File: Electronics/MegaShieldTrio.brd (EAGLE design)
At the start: 99.8 x 80 mm, 29 parts, among them J2 RJ11-2L-B, X1 RJ45-6L21-B, X2 Cruise

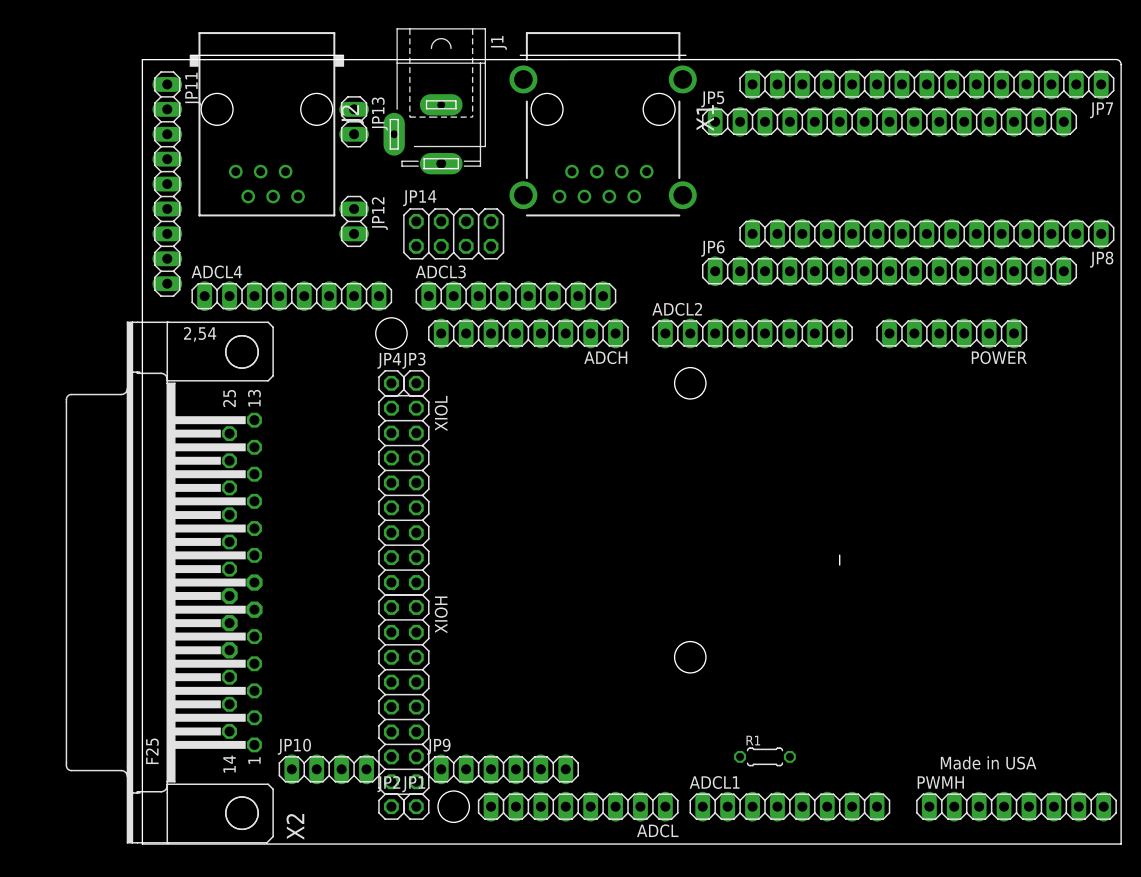
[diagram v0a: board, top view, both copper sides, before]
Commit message: New sonar board; trio modified to match
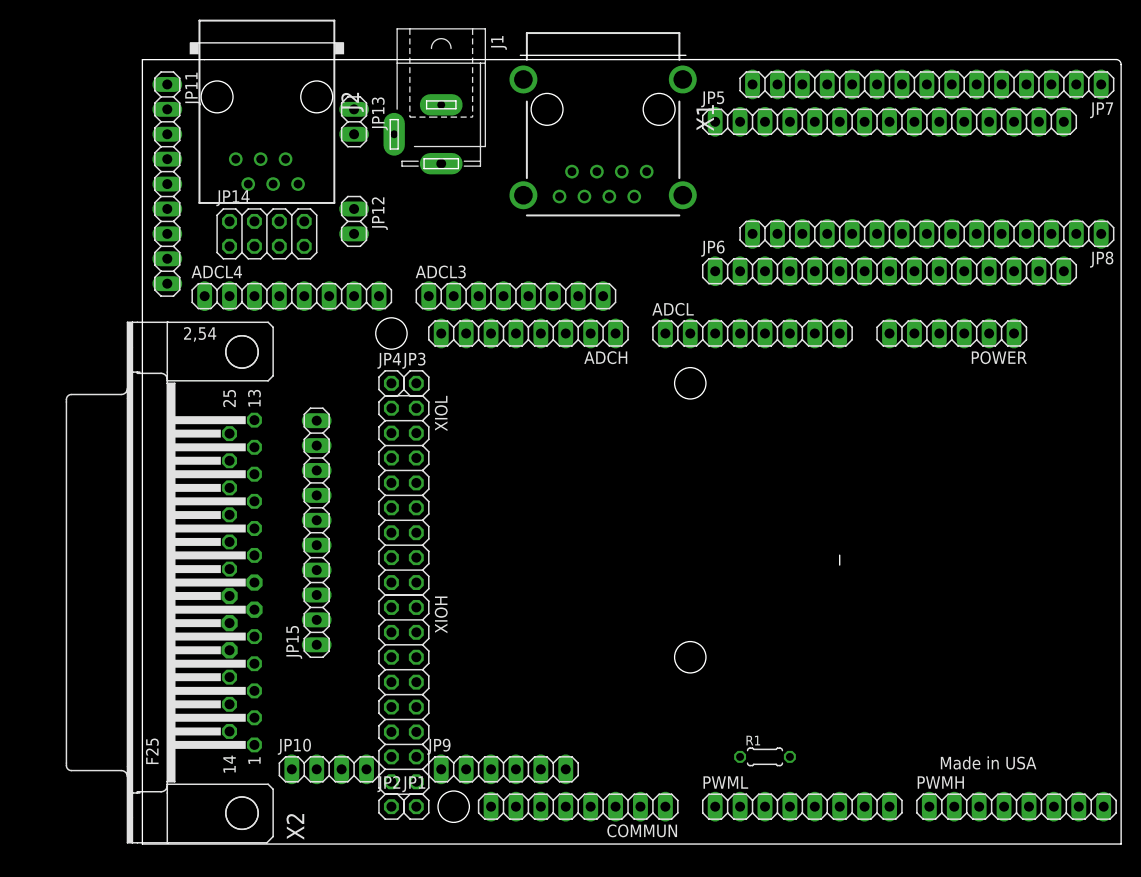
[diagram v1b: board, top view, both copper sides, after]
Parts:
- removed ADCL1: Digital 0-7, pinhead:1X08
- removed ADCL2: Analog In 0-7, pinhead:1X08
- added COMMUN: Digital 14-21, pinhead:1X08
- added JP15: (no value), pinhead:1X10
- added PWML: Digital 0-7, pinhead:1X08
- ADCL: value Digital 14-21 -> Analog In 0-7
- moved ADCL 51.4 mm to (62.2, 52.1), turned to 0 degrees
- moved JP14 19.1 mm to (12.7, 62.2)
- moved J2 1.27 mm to (12.7, 76.2)
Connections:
- new net N$2: COMMUN.2, PWML.3
- new net N$9: COMMUN.1, PWML.4
- net +5V: now also X1.1; no longer X1.2
- net A6: now also COMMUN.7; no longer ADCL.7
- net D3INT1: now also COMMUN.8; no longer ADCL.8
- net GND: now also X1.4; no longer X1.1
- net N$1: now also PWML.1; no longer ADCL1.1
- net N$11: now also COMMUN.4; no longer ADCL.4
- net N$25: now also ADCL.5, X1.7; no longer ADCL2.5, X1.5
- net N$26: now also ADCL.6, X1.3; no longer ADCL2.6, X1.6
- net N$33: now also COMMUN.3; no longer ADCL.3
- net N$34: now also ADCL.7, X1.5; no longer ADCL2.7, X1.7
- net N$35: now also ADCL.8; no longer ADCL2.8
- net N$36: now also X1.2; no longer X1.3
- net N$37: now also PWML.2; no longer ADCL1.2
- net N$7: now also ADCL.4, X1.6; no longer ADCL2.4, X1.4

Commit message: Parts match physical size
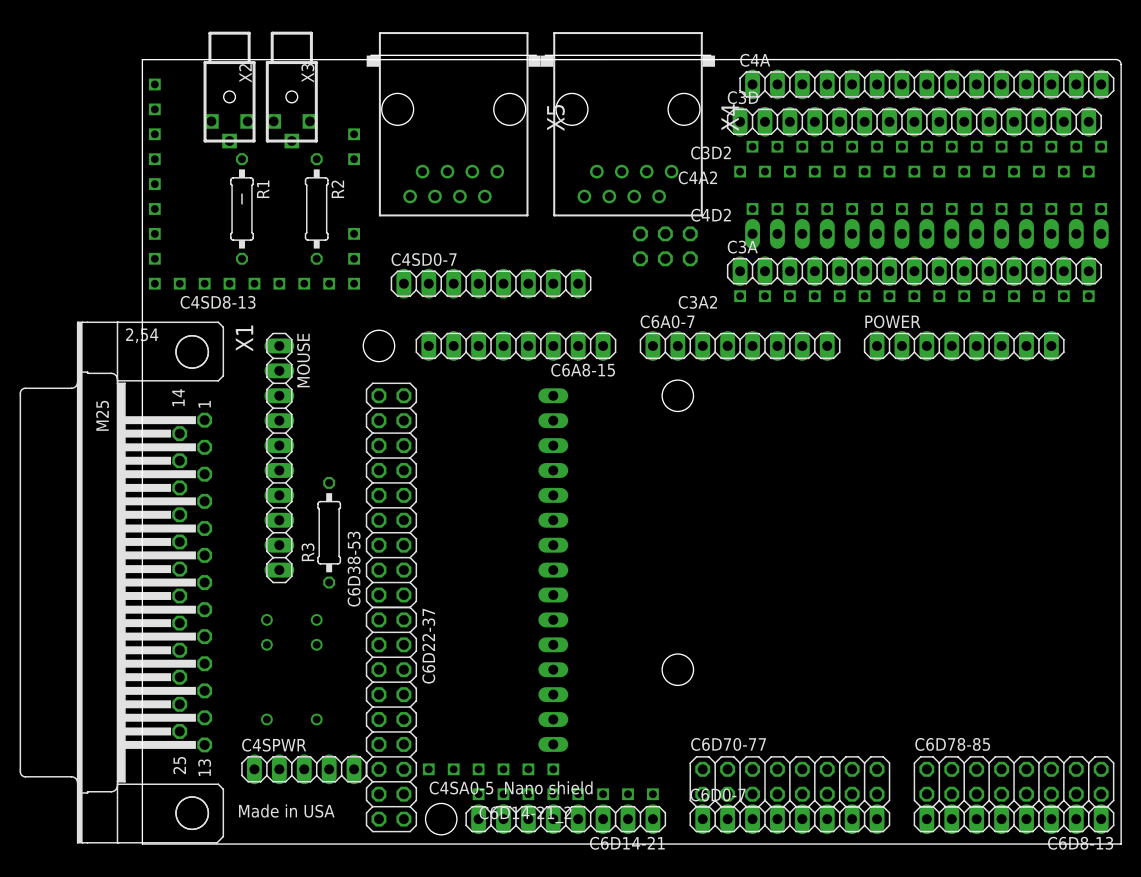
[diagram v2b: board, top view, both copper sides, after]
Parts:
- removed ADCH: Analog In 8-15, pinhead:1X08
- removed ADCL: Analog In 0-7, pinhead:1X08
- removed ADCL3, PWML: Digital 0-7, pinhead:1X08
- removed ADCL4, PWMH: Digital 8-13, pinhead:1X08
- removed COMMUN: Digital 14-21, pinhead:1X08
- removed J1: (no value), con-jack:SPC4077
- removed J2: RJ11-2L-B, con-tycoelectronics:RJ11-NO_SHIELD
- removed JP1, JP2: 5V, pinhead:1X01
- removed JP10: (no value), pinhead:1X04
- removed JP11: (no value), pinhead:1X09
- removed JP12, JP13: (no value), pinhead:1X02
- removed JP14: (no value), pinhead:2X04
- removed JP15: (no value), pinhead:1X10
- removed JP3, JP4: GND, pinhead:1X01
- removed JP5: C3 Digital, pinhead:1X15
- removed JP6: C3 Analog, pinhead:1X15
- removed JP9: (no value), pinhead:1X06
- removed XIOH: Digital 22-37, pinhead:2X08
- removed XIOL: Digital 38-53, pinhead:2X08
- added C3A: C3 Analog, pinhead:1X15
- added C3A2, C3D2, C4A2, C4D2: 1X15HEADER, Elcano:1X15HEADER
- added C3D: C3 Digital, pinhead:1X15
- added C4SA0-5: Nano shield, Elcano:1X6HEADER
- added C4SD0-7: Nano shield, pinhead:1X08
- added C4SD8-13: Nano shield, Elcano:1X8HEADER
- added C4SPWR: Nano shield, pinhead:1X05
- added C5A: C5 Analog, pinhead:1X15
- added C6A0-7: C6 Analog In 0-7, pinhead:1X08
- added C6A8-15: C6 Analog In 8-15, pinhead:1X08
- added C6D0-7: GPS, pinhead:1X08
- added C6D14-21: C6 Digital 14-21, pinhead:1X08
- added C6D14-21_2: C5D, Elcano:1X8HEADER
- added C6D22-37: C6 Digital 22-37, pinhead:2X09
- added C6D38-53: C6 Digital 38-53, pinhead:2X09
- added C6D70-77, C6D78-85: Max32, pinhead:2X08
- added C6D8-13: C6D8-13, pinhead:1X08
- added ICSP: (no value), pinhead:2X03
- added MOUSE: Visual odometry, pinhead:1X10
- added R2, R3: 1 M, rcl:0207/10
- added RL1: V23040--B201TSC, Elcano:TSC-112L3H
- added U$4: CHR_UM6, Elcano:CHR_UM6
- added X3: ODO_JACK, Elcano:ODO_JACK
- added X4, X5: RJ45-8L-B, con-tycoelectronics:RJ45-NO-SHIELD
- C4A: value C4 Digital -> C4 Analog
- C4D: value C4 Analog -> C4 Digital
- POWER: value POWER -> C6 Power; device pinhead:1X06 -> pinhead:1X08
- R1: value 1M -> 1 M; device rcl:0204/5 -> rcl:0207/10
- X1: value RJ45-6L21-B -> Vehicle control; device con-tycoelectronics:RJ45-SHIELD1 -> con-subd:M25H
- X2: value Cruise -> ODO_JACK; device con-subd:F25H -> Elcano:ODO_JACK
- moved R1 77.3 mm to (10.2, 64.8), turned to 270 degrees
- moved X1 63.9 mm to (5.08, 26.7), turned to 270 degrees
- moved X2 49.5 mm to (8.89, 76.2), turned to 270 degrees
- moved POWER 1.80 mm to (83.8, 50.8), turned to 0 degrees
- turned C4A to 0 degrees
- flipped C4D to the bottom
- renumbered JP7 to C4A, JP8 to C4D
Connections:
- removed net A12: JP6.5, PWMH.1, X2.10
- removed net A13: ADCH.6, JP5.14, X2.6
- removed net A14: ADCH.7, JP5.13, X2.7
- removed net A15: ADCH.8, JP5.12, X2.8
- removed net A6: COMMUN.7, X2.23
- removed net D23: X2.5, XIOH.15
- removed net D27: JP6.15, X2.4, XIOH.11
- removed net D29: ADCL4.6, C4D.15, X2.3, XIOH.9
- removed net D31: X2.2, XIOH.7
- removed net D33: X2.1, XIOH.5
- removed net D35: JP14.7, X2.15, XIOH.3
- removed net D36: X2.13, XIOH.2
- removed net D37: X2.16, XIOH.1
- removed net D3INT1: COMMUN.8, J1.3, R1.2, X2.21
- removed net D43: XIOL.11
- removed net D49: J2.1, XIOL.5
- removed net D53: J2.3, XIOL.1
- removed net D9: JP6.6, PWMH.2
- removed net N$1: PWML.1, X2.19
- removed net N$2: COMMUN.2, PWML.3
- removed net N$27: ADCL4.8, C4D.13
- removed net N$6: J2.4, XIOL.2
- new net AREF: C3A.13, C3A2.P$13, C4A.13, C4A2.P$13, C4SD8-13.P$1, C5A.13, C6D8-13.1
- new net CRS_BRAKE: C3D.13, C3D2.P$13, C5A.6, C6A8-15.7, X1.7
- new net CRS_DRIVE_CMD: C3D.2, C3D2.P$2, X1.18
- new net CRS_REVERSE: C3D.11, C3D2.P$11, C6D22-37.2, X1.13
- new net CRS_STEER: C3D.14, C3D2.P$14, C5A.7, C6A8-15.6, X1.6
- new net CRS_THROTTLE: C3D.12, C3D2.P$12, C5A.5, C6A8-15.8, X1.8
- new net DIRECTION: C3A.6, C3A2.P$6
- new net HORIZ: C4A.5, C4A2.P$5, C4SA0-5.P$1
- new net LED1: C6D22-37.15, X1.5
- new net LED3: C3A.15, C3A2.P$15, C6D22-37.11, X1.4
- new net LED4: C4A.15, C4A2.P$15, C4SD8-13.P$3, C6D22-37.9, X1.3
- new net LED5: C6D22-37.7, X1.2
- new net LED6: C6D22-37.5, X1.1
- new net LED7: C6D22-37.3, X1.15
- new net LED8: C6D22-37.1, X1.16
- new net MISO: C6D38-53.13, ICSP.1, MOUSE.5, U$4.D4
- new net MOSI: C6D38-53.14, ICSP.4, MOUSE.6, U$4.D3
- new net MOUSE_LED: C6D38-53.12, MOUSE.10
- new net MOUSE_SS: C6D38-53.16, MOUSE.4
- new net N$29: C3D.9, C3D2.P$9, RL1.COIL2
- new net N$30: C6D78-85.7, C6D78-85.8
- new net N$31: C6D78-85.10, C6D78-85.9
- new net N$32: RL1.COM2, X4.1, X5.1
- new net N$39: C6D78-85.15, C6D78-85.16
- new net N$41: C6D70-77.1, C6D70-77.2
- new net N$42: C6D0-7.6, C6D14-21.2, C6D14-21_2.P$7, U$4.D2
- new net N$43: C6D14-21.6, C6D14-21_2.P$3, U$4.TX
- new net N$44: C6D70-77.3, C6D70-77.4
- new net N$45: C6D70-77.5, C6D70-77.6
- new net N$46: C6D70-77.7, C6D70-77.8
- new net N$47: C6D70-77.10, C6D70-77.9
- new net N$48: C6D70-77.11, C6D70-77.12
- new net N$49: C6D70-77.13, C6D70-77.14
- new net N$50: C6D70-77.15, C6D70-77.16
- new net N$52: C4A.14, C4A2.P$14
- new net N$54: C3D.6, C3D2.P$6
- new net N$55: C3D.10, C3D2.P$10
- new net N$56: C3A.1, C3A2.P$1, C5A.1, C6D22-37.13, POWER.1
- new net N$57: C3A.7, C3A2.P$7
- new net N$59: C3A.14, C3A2.P$14
- new net NPD: C6D38-53.10, MOUSE.9
- new net PRESENCE: C4A.8, C4A2.P$8, C4SA0-5.P$4
- new net RX0: C6D0-7.8, X1.22
- new net SCK: C6D38-53.15, ICSP.3, MOUSE.7, U$4.D5
- new net SIZE: C4A.7, C4A2.P$7, C4SA0-5.P$3
- new net SPEED: C3A.5, C3A2.P$5, C6D8-13.7, X1.10
- new net SPEED_LIMIT: C4D.7, C4D2.P$7, C4SD0-7.5, X1.9
- new net TILT_SS: C6D38-53.8, U$4.D6
- new net TX0: C6D0-7.7, X1.20
- new net VBIT0: C4D.8, C4D2.P$8, C4SD0-7.6, C6D38-53.3
- new net VBIT1: C4D.9, C4D2.P$9, C4SD0-7.7, C6D38-53.5
- new net VBIT2: C4D.10, C4D2.P$10, C4SD0-7.8, C6D38-53.7
- new net VBIT3: C4D.11, C4D2.P$11, C4SD8-13.P$8, C6D38-53.9
- new net VERT: C4A.6, C4A2.P$6, C4SA0-5.P$2
- new net VIS_VALID: C4D.15, C4D2.P$15, C4SD8-13.P$4, C6D38-53.11
- new net WHEEL_CLICK: C6D14-21.8, C6D14-21_2.P$1, R2.1, X1.21, X3.P$1
- new net WIRELESS: C6D14-21.7, C6D14-21_2.P$2, R1.1, X1.14, X2.P$1
- net +5V: now also C3A.4, C3A2.P$4, C4A.4, C4A2.P$4, C4SPWR.3, C5A.4, C6D22-37.17, C6D22-37.18, ICSP.2, MOUSE.2, POWER.4, R1.2, R2.2, R3.2, RL1.NO, U$4.VIN, X1.24; no longer C4D.4, JP1.1, JP10.3, JP2.1, JP6.4, POWER.3, R1.1, X1.1, X2.24
- net D39: now also C6D38-53.2, X1.12; no longer X2.12, XIOL.15
- net D41: now also C6D38-53.4, X1.11; no longer X2.11, XIOL.13
- net GND: now also C3A.2, C3A2.P$2, C3D.4, C3D2.P$4, C4A.2, C4A2.P$2, C4D.4, C4D2.P$4, C4SD8-13.P$2, C4SPWR.4, C4SPWR.5, C5A.2, C6D38-53.17, C6D38-53.18, C6D8-13.2, ICSP.6, MOUSE.1, POWER.2, POWER.3, U$4.GND, U$4.GND2, X1.25, X2.P$2, X2.P$3, X3.P$2, X3.P$3, X4.4, X5.4; no longer ADCL4.7, C4A.4, C4D.2, J1.1, J1.2, J2.6, JP10.4, JP3.1, JP4.1, JP5.4, JP6.2, POWER.4, POWER.5, PWMH.7, X1.4, X2.25
- net N$10: now also C3D.1, C3D2.P$1, C4D.2, C4D2.P$2, C4SD0-7.2; no longer ADCL3.2, C4A.2, JP5.1
- net N$11: now also C4D.5, C4D2.P$5, C4SD0-7.3, C6D14-21.4, C6D14-21_2.P$5; no longer ADCL3.3, C4A.5, COMMUN.4
- net N$12: now also C3D.5, C3D2.P$5, C4D.6, C4D2.P$6, C4SD0-7.4; no longer ADCL3.4, C4A.6, JP5.5
- net N$13: now also C3D.7, C3D2.P$7, X5.2; no longer ADCL3.5, C4A.7
- net N$14: now also C5A.11, C6A8-15.2, X5.7; no longer J2.2, XIOL.3
- net N$15: now also C5A.10, C6A8-15.3, X5.6; no longer JP5.2, X2.18
- net N$16: now also C5A.9, C6A8-15.4, X5.5; no longer C4D.5, JP14.2, JP9.1
- net N$17: now also C6D14-21.5, C6D14-21_2.P$4, U$4.RX; no longer ADCL3.8, C4A.10
- net N$18: now also C5A.8, C6A8-15.5, X5.3; no longer ADCL4.1, C4A.11
- net N$19: now also C4D.12, C4D2.P$12, C4SD8-13.P$7, C6A0-7.3; no longer ADCL4.2, C4A.12, JP14.1
- net N$20: now also C4D.14, C4D2.P$14, C4SD8-13.P$5, C6A0-7.1; no longer ADCL4.4, C4A.14, JP14.5
- net N$21: now also C5A.12, C6A8-15.1, X5.8; no longer C4D.6, JP14.4, JP9.2
- net N$22: now also C4A.1, C4A2.P$1; no longer C4D.7, JP14.6, JP9.3
- net N$23: now also C6D78-85.1, C6D78-85.2; no longer ADCL4.5, C4A.15
- net N$24: now also C6D78-85.3, C6D78-85.4; no longer C4D.8, JP14.8, JP9.4
- net N$25: now also C3A.9, C3A2.P$9, C4A.9, C4A2.P$9, C4SA0-5.P$5, C6A0-7.5, X4.7; no longer ADCL.5, C4D.9, JP6.9, JP9.5, X1.7
- net N$26: now also C3A.10, C3A2.P$10, C4A.10, C4A2.P$10, C4SA0-5.P$6, C6A0-7.6, X4.3; no longer ADCL.6, C4D.10, JP6.10, JP9.6, X1.3
- net N$28: now also C6D78-85.5, C6D78-85.6; no longer C4D.14, JP10.2
- net N$3: now also C4D.13, C4D2.P$13, C4SD8-13.P$6, C6A0-7.2; no longer ADCL4.3, C4A.13, JP14.3
- net N$33: now also C4D.1, C4D2.P$1, C4SD0-7.1, C6D14-21.3, C6D14-21_2.P$6; no longer ADCL3.1, C4A.1, COMMUN.3
- net N$34: now also C3A.11, C3A2.P$11, C4A.11, C4A2.P$11, C6A0-7.7, X4.5; no longer ADCL.7, C4D.11, JP6.11, X1.5
- net N$35: now also C3A.12, C3A2.P$12, C4A.12, C4A2.P$12, C6A0-7.8, X4.8; no longer ADCL.8, C4D.12, JP6.12, X1.8
- net N$36: now also C3D.8, C3D2.P$8, X4.2; no longer JP5.8, X1.2
- net N$37: now also C6D78-85.11, C6D78-85.12; no longer PWML.2, X2.20
- net N$38: now also C6D78-85.13, C6D78-85.14; no longer ADCL3.7, C4A.9
- net N$4: now also C3D.15, C3D2.P$15, C6D22-37.16, X1.17; no longer JP5.15, X2.17, XIOH.16
- net N$5: now also C4SPWR.2, MOUSE.3, POWER.5, RL1.NC; no longer ADCH.1, ADCL3.6, C4A.8, X2.9
- net N$7: now also C3A.8, C3A2.P$8, C6A0-7.4, X4.6; no longer ADCL.4, JP6.8, X1.6
- net N$8: now also R3.1, RL1.COIL1; no longer J2.5, XIOL.4
- net N$9: now also C6D0-7.5, C6D14-21.1, C6D14-21_2.P$8, U$4.D1; no longer COMMUN.1, PWML.4
- net RESET: now also C3A.3, C3A2.P$3, C3D.3, C3D2.P$3, C4A2.P$3, C4D2.P$3, C4SPWR.1, C5A.3, ICSP.5, MOUSE.8, POWER.6; no longer JP10.1, JP5.3, JP6.3, POWER.1
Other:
- outline, holes or cut-outs redrawn

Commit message: Rearranged signals
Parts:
- added JP1, JP2, JP3: (no value), jumper:JP2
- added JP4: (no value), Elcano:1X8HEADER
- ICSP: value (none) -> C6
- moved R3 7.62 mm to (19.1, 39.4)
- moved C3D2 1.27 mm to (78.7, 71.1)
- moved C4A2 1.27 mm to (80.0, 68.6)
- moved RL1 1.27 mm to (16.5, 12.7)
- turned C5A to 90 degrees
- turned C6A8-15 to 0 degrees
- turned C6D0-7 to 180 degrees
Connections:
- net N$17 renamed INU_CNTRL
- net N$32 renamed SNR_PWR
- net N$43 renamed INU_BRN
- removed net CRS_BRAKE: C3D.13, C3D2.P$13, C5A.6, C6A8-15.7, X1.7
- removed net CRS_DRIVE_CMD: C3D.2, C3D2.P$2, X1.18
- removed net CRS_REVERSE: C3D.11, C3D2.P$11, C6D22-37.2, X1.13
- removed net CRS_STEER: C3D.14, C3D2.P$14, C5A.7, C6A8-15.6, X1.6
- removed net CRS_THROTTLE: C3D.12, C3D2.P$12, C5A.5, C6A8-15.8, X1.8
- removed net DIRECTION: C3A.6, C3A2.P$6
- removed net HORIZ: C4A.5, C4A2.P$5, C4SA0-5.P$1
- removed net MOUSE_LED: C6D38-53.12, MOUSE.10
- removed net N$10: C3D.1, C3D2.P$1, C4D.2, C4D2.P$2, C4SD0-7.2
- removed net N$11: C4D.5, C4D2.P$5, C4SD0-7.3, C6D14-21.4, C6D14-21_2.P$5
- removed net N$12: C3D.5, C3D2.P$5, C4D.6, C4D2.P$6, C4SD0-7.4
- removed net N$13: C3D.7, C3D2.P$7, X5.2
- removed net N$14: C5A.11, C6A8-15.2, X5.7
- removed net N$15: C5A.10, C6A8-15.3, X5.6
- removed net N$16: C5A.9, C6A8-15.4, X5.5
- removed net N$18: C5A.8, C6A8-15.5, X5.3
- removed net N$19: C4D.12, C4D2.P$12, C4SD8-13.P$7, C6A0-7.3
- removed net N$20: C4D.14, C4D2.P$14, C4SD8-13.P$5, C6A0-7.1
- removed net N$21: C5A.12, C6A8-15.1, X5.8
- removed net N$22: C4A.1, C4A2.P$1
- removed net N$25: C3A.9, C3A2.P$9, C4A.9, C4A2.P$9, C4SA0-5.P$5, C6A0-7.5, X4.7
- removed net N$26: C3A.10, C3A2.P$10, C4A.10, C4A2.P$10, C4SA0-5.P$6, C6A0-7.6, X4.3
- removed net N$29: C3D.9, C3D2.P$9, RL1.COIL2
- removed net N$3: C4D.13, C4D2.P$13, C4SD8-13.P$6, C6A0-7.2
- removed net N$33: C4D.1, C4D2.P$1, C4SD0-7.1, C6D14-21.3, C6D14-21_2.P$6
- removed net N$34: C3A.11, C3A2.P$11, C4A.11, C4A2.P$11, C6A0-7.7, X4.5
- removed net N$35: C3A.12, C3A2.P$12, C4A.12, C4A2.P$12, C6A0-7.8, X4.8
- removed net N$36: C3D.8, C3D2.P$8, X4.2
- removed net N$42: C6D0-7.6, C6D14-21.2, C6D14-21_2.P$7, U$4.D2
- removed net N$52: C4A.14, C4A2.P$14
- removed net N$54: C3D.6, C3D2.P$6
- removed net N$55: C3D.10, C3D2.P$10
- removed net N$56: C3A.1, C3A2.P$1, C5A.1, C6D22-37.13, POWER.1
- removed net N$57: C3A.7, C3A2.P$7
- removed net N$59: C3A.14, C3A2.P$14
- removed net N$9: C6D0-7.5, C6D14-21.1, C6D14-21_2.P$8, U$4.D1
- removed net PRESENCE: C4A.8, C4A2.P$8, C4SA0-5.P$4
- removed net RX0: C6D0-7.8, X1.22
- removed net SIZE: C4A.7, C4A2.P$7, C4SA0-5.P$3
- removed net SPEED_LIMIT: C4D.7, C4D2.P$7, C4SD0-7.5, X1.9
- removed net TILT_SS: C6D38-53.8, U$4.D6
- removed net TX0: C6D0-7.7, X1.20
- removed net VBIT2: C4D.10, C4D2.P$10, C4SD0-7.8, C6D38-53.7
- removed net VBIT3: C4D.11, C4D2.P$11, C4SD8-13.P$8, C6D38-53.9
- removed net VERT: C4A.6, C4A2.P$6, C4SA0-5.P$2
- removed net VIS_VALID: C4D.15, C4D2.P$15, C4SD8-13.P$4, C6D38-53.11
- removed net WHEEL_CLICK: C6D14-21.8, C6D14-21_2.P$1, R2.1, X1.21, X3.P$1
- removed net WIRELESS: C6D14-21.7, C6D14-21_2.P$2, R1.1, X1.14, X2.P$1
- new net 3.3V: C3A.14, C3A2.P$14, C4A.14, C4A2.P$14, C4SPWR.2, MOUSE.3, POWER.5, RL1.NC
- new net 4D5_6A14: C4D.8, C4D2.P$8, C4SD0-7.6
- new net 4D6_6A15: C4D.9, C4D2.P$9, C4SD0-7.7
- new net 4D7_6D43: C4D.10, C4D2.P$10, C4SD0-7.8, C6D38-53.6
- new net 6D10_2A6: C6D8-13.6, X1.23
- new net C2STAT: C6D14-21.4, C6D14-21_2.P$5, X1.19
- new net C4AVL: C3D.5, C3D2.P$5, C4D.6, C4D2.P$6, C4SD0-7.4, C6D22-37.3
- new net C4D11: C4D.14, C4D2.P$14, C4SD8-13.P$5
- new net C4D12: C4D.15, C4D2.P$15, C4SD8-13.P$4
- new net C6AVL: C4D.5, C4D2.P$5, C4SD0-7.3, C6D22-37.16
- new net C6D29: C6D22-37.10, JP4.P$1
- new net C6D31: C6D22-37.8, JP4.P$2
- new net C6D33: C6D22-37.6, JP4.P$3
- new net C6D35: C6D22-37.4, JP4.P$4
- new net C6D37: C6D22-37.2, JP4.P$5
- new net CHN1: C3D.7, C3D2.P$7, C6D38-53.1, X4.2
- new net CHN2: C3D.6, C3D2.P$6, C6D22-37.1, X5.2
- new net CLICK1: C6D0-7.6, R2.1, X1.21, X3.P$1
- new net CLICK2: C6D0-7.5, R1.1, X1.14, X2.P$1
- new net CRS_BRK: C3D.8, C3D2.P$8, C6A0-7.6, C6D0-7.3, C6D38-53.3, X1.7
- new net CRS_REV: C3D.11, C3D2.P$11, C6D38-53.9, X1.13
- new net CRS_STR: C3D.9, C3D2.P$9, C6A0-7.7, C6D38-53.5, X1.6
- new net CRS_THR: C3D.12, C3D2.P$12, C6A0-7.8, C6D38-53.11, C6D38-53.8, X1.8
- new net DRV_CMD: C3D.1, C3D2.P$1, C6D22-37.11, X1.18
- new net F2RNG: C3A.10, C3A2.P$10, C4A.10, C4A2.P$10, C4SA0-5.P$6, C5A.5, C6A8-15.8, X5.4
- new net FL2RNG: C5A.6, C6A8-15.7, X5.5
- new net FL_RNG: C3A.6, C3A2.P$6, C4A.6, C4A2.P$6, C4SA0-5.P$2, C6A0-7.2, X4.5
- new net FR2RNG: C5A.7, C6A8-15.6, X5.6
- new net FR_RNG: C3A.7, C3A2.P$7, C4A.7, C4A2.P$7, C4SA0-5.P$3, C6A0-7.3, X4.6
- new net F_RNG: C3A.5, C3A2.P$5, C4A.5, C4A2.P$5, C4SA0-5.P$1, C5A.10, C6A0-7.1, X4.4
- new net GPS_CNTRL: C6D14-21.1, C6D14-21_2.P$8, U$4.D1
- new net GPS_LOC: C6D14-21.2, C6D14-21_2.P$7, U$4.D2
- new net GPS_PWR: C6D8-13.7
- new net INU_SS: C6D22-37.12, U$4.D6
- new net L2RNG: C3A.11, C3A2.P$11, C4A.11, C4A2.P$11, C5A.8, X5.7
- new net L_RNG: C3A.8, C3A2.P$8, C4A.8, C4A2.P$8, C4SA0-5.P$4, C5A.11, C6A0-7.4, X4.7
- new net MOV_OK: C3D.13, C3D2.P$13, C4SD0-7.5, C6D0-7.4, JP3.3, X1.17
- new net N$1: C4A.3, C4A2.P$3, C4D.3, C4D2.P$3, C4SPWR.1
- new net N$2: C4D.7, C4D2.P$7
- new net N$6: C6D38-53.17, JP2.2
- new net NAV_FIX: C4D.2, C4D2.P$2, C4SD0-7.1, C6D14-21.3, C6D14-21_2.P$6
- new net PATH: C3D.2, C3D2.P$2, C4D.1, C4D2.P$1, C4SD0-7.2, C6D22-37.9
- new net PWR_SEL: C3D.10, C3D2.P$10, C6D38-53.7, RL1.COIL2
- new net R2RNG: C3A.12, C3A2.P$12, C4A.12, C4A2.P$12, C5A.9, C6A8-15.4, X5.8
- new net R_RNG: C3A.9, C3A2.P$9, C4A.9, C4A2.P$9, C4SA0-5.P$5, C5A.12, C6A0-7.5, X4.8
- new net SPD_LMT: C4D.12, C4D2.P$12, C4SD8-13.P$7, X1.9
- new net VIN: C3A.1, C3A2.P$1, C4A.1, C4A2.P$1, C5A.1, C6D22-37.14, POWER.1
- new net VIS_IN: X1.20
- new net VIS_OUT: C6D0-7.7, X1.22
- net +5V: no longer C5A.4, R3.2
- net D39: now also C3D.15, C3D2.P$15, C4D.13, C4D2.P$13, C4SD8-13.P$6, JP4.P$6
- net D41: now also C4D.11, C4D2.P$11, C4SD8-13.P$8, JP2.3, JP4.P$7
- net GND: now also C6D22-37.5, JP2.1, X4.3, X5.3; no longer C6D38-53.17, X4.4, X5.4
- net LED1: now also C6D8-13.8; no longer C6D22-37.15
- net LED3: no longer C6D22-37.11
- net LED4: no longer C6D22-37.9
- net LED5: now also C5A.15, C6D38-53.12, MOUSE.10; no longer C6D22-37.7
- net LED6: now also C6D22-37.13; no longer C6D22-37.5
- net LED7: now also C6D22-37.15; no longer C6D22-37.3
- net LED8: now also C6D14-21.8, C6D14-21_2.P$1; no longer C6D22-37.1
- net MISO: now also C6D8-13.4, JP3.1; no longer C6D38-53.13
- net MOSI: now also C6D8-13.5
- net N$4: now also C6D38-53.15, JP1.2; no longer C3D.15, C3D2.P$15, C6D22-37.16, X1.17
- net N$5: now also C6D38-53.13, JP3.2; no longer C4SPWR.2, MOUSE.3, POWER.5, RL1.NC
- net N$7: now also C6D14-21.7, C6D14-21_2.P$2; no longer C3A.8, C3A2.P$8, C6A0-7.4, X4.6
- net RESET: now also C6D22-37.7; no longer C4A.3, C4A2.P$3, C4D.3, C4D2.P$3, C4SPWR.1
- net SCK: now also C6D8-13.3, JP1.1; no longer C6D38-53.15
- net SPEED: now also C3D.14, C3D2.P$14, C6A8-15.3, JP1.3; no longer C3A.5, C3A2.P$5, C6D8-13.7
- net VBIT0: now also C6A8-15.2; no longer C4D.8, C4D2.P$8, C4SD0-7.6, C6D38-53.3
- net VBIT1: now also C6A8-15.1; no longer C4D.9, C4D2.P$9, C4SD0-7.7, C6D38-53.5

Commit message: Power and ground traces
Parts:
- JP1: value (none) -> D52/12
- JP2: value (none) -> D50/11
- JP3: value (none) -> D48/10
- JP4: value (none) -> Spares
- moved JP1 3.81 mm to (34.3, 47.0)
- moved JP2 3.81 mm to (34.3, 43.2)
- moved R3 2.54 mm to (19.1, 41.9)
- flipped C6D22-37 to the bottom
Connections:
- removed net GPS_PWR: C6D8-13.7
- removed net N$1: C4A.3, C4A2.P$3, C4D.3, C4D2.P$3, C4SPWR.1
- removed net N$2: C4D.7, C4D2.P$7
- removed net VBIT0: C6A8-15.2
- removed net VBIT1: C6A8-15.1
- new net N$3: C6D38-53.6, JP4.P$8
- net +5V: now also R3.2
- net 4D5_6A14: now also C6A8-15.2
- net 4D6_6A15: now also C6A8-15.1
- net 4D7_6D43: no longer C6D38-53.6
- net CRS_STR: now also C6D0-7.2
- net D41: now also JP1.3; no longer JP2.3
- net GND: now also JP1.1; no longer JP2.1
- net L2RNG: now also C6A8-15.5
- net MOV_OK: now also C4D.7, C4D2.P$7
- net N$4: now also JP2.2; no longer JP1.2
- net N$6: now also JP1.2; no longer JP2.2
- net RESET: now also C4A.3, C4A2.P$3, C4D.3, C4D2.P$3, C4SPWR.1
- net SCK: now also JP2.1; no longer JP1.1
- net SPEED: now also JP2.3; no longer JP1.3
- net VIS_IN: now also C6D0-7.8
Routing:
- net GND: track 0.00 -> 396.7 mm, vias 0 -> 2
- net +5V: track 0.00 -> 253.0 mm, vias 0 -> 2
- net RESET: track 0.00 -> 23.0 mm
- net D39: track 0.00 -> 7.62 mm
- net C4AVL: track 0.00 -> 5.69 mm
- net NAV_FIX: track 0.00 -> 5.08 mm
- net D41: track 0.00 -> 5.08 mm
- net PATH: track 0.00 -> 5.08 mm
- net MOV_OK: track 0.00 -> 5.08 mm
- net N$7: track 0.00 -> 2.54 mm
- net LED8: track 0.00 -> 2.54 mm
- net INU_CNTRL: track 0.00 -> 2.54 mm
- net INU_BRN: track 0.00 -> 2.54 mm
- net GPS_LOC: track 0.00 -> 2.54 mm
- net GPS_CNTRL: track 0.00 -> 2.54 mm
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
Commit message: Routed
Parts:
- C6D14-21: device pinhead:1X08 -> Elcano:1X8HEADER
- moved C6D14-21 9.02 mm to (52.2, 2.54)
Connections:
- net C2STAT: now also C6D14-21.P$4; no longer C6D14-21.4
- net GPS_CNTRL: now also C6D14-21.P$1; no longer C6D14-21.1
- net GPS_LOC: now also C6D14-21.P$2; no longer C6D14-21.2
- net INU_BRN: now also C6D14-21.P$6; no longer C6D14-21.6
- net INU_CNTRL: now also C6D14-21.P$5; no longer C6D14-21.5
- net LED8: now also C6D14-21.P$8; no longer C6D14-21.8
- net N$7: now also C6D14-21.P$7; no longer C6D14-21.7
- net NAV_FIX: now also C6D14-21.P$3; no longer C6D14-21.3
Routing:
- net MOV_OK: track 5.08 -> 274.6 mm, vias 0 -> 11
- net SCK: track 0.00 -> 245.7 mm, vias 0 -> 9
- net SPD_LMT: track 2.54 -> 225.8 mm, vias 0 -> 5
- net RESET: track 23.0 -> 244.0 mm, vias 0 -> 13
- net CRS_BRK: track 2.54 -> 210.5 mm, vias 0 -> 11
- net AREF: track 2.54 -> 209.8 mm, vias 0 -> 4
- net D39: track 7.62 -> 210.2 mm, vias 0 -> 6
- net LED4: track 0.00 -> 199.3 mm, vias 0 -> 7
- net 3.3V: track 2.54 -> 199.4 mm, vias 0 -> 6
- net SPEED: track 2.54 -> 197.1 mm, vias 0 -> 7
- net MISO: track 0.00 -> 191.2 mm, vias 0 -> 3
- net R2RNG: track 2.54 -> 193.7 mm, vias 0 -> 8
- net CRS_STR: track 2.54 -> 192.5 mm, vias 0 -> 9
- net LED1: track 0.00 -> 189.8 mm, vias 0 -> 10
- net MOSI: track 0.00 -> 189.8 mm, vias 0 -> 12
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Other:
- outline, holes or cut-outs redrawn
